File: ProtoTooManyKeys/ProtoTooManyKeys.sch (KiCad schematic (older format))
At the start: 74 parts, among them J1 54104-3031_Oled, J2 AVR-ISP-6, SW1 SW_Push, U1 PRTR5V0U2X, U2 AT90USB1286-AU, U3 PCA9306TDCURQ1, U4 AZ1117CH-3.3TRG1, Y1 16MHz

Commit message: Routing finished
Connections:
- net ROW0: now also U2.34 (PE1); no longer U2.50 (PA1)
- net ROW1: now also U2.33 (PE0); no longer U2.49 (PA2)
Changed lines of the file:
@@
 Text GLabel 4200 4200 2    50   Input ~ 0
 SDA
-Text GLabel 4200 1600 2    50   Input ~ 0
+Text GLabel 2800 3200 0    50   Input ~ 0
 ROW1
-Text GLabel 4200 1500 2    50   Input ~ 0
+Text GLabel 2800 3300 0    50   Input ~ 0
 ROW0
 Text GLabel 4200 3200 2    50   Input ~ 0
@@
 $EndComp
 Wire Wire Line
-	4200 1500 4100 1500
-Wire Wire Line
-	4200 1600 4100 1600
+	2800 3300 2900 3300
+Wire Wire Line
+	2800 3200 2900 3200
 Text GLabel 10350 2400 0    50   Input ~ 0
 RESET
@@
 NoConn ~ 4100 3800
 NoConn ~ 4100 3900
-NoConn ~ 2900 3200
-NoConn ~ 2900 3300
 NoConn ~ 2900 3800
 NoConn ~ 2900 3900
@@
 	1    0    0    -1
 $EndComp
+NoConn ~ 4100 1500
+NoConn ~ 4100 1600
 $EndSCHEMATC

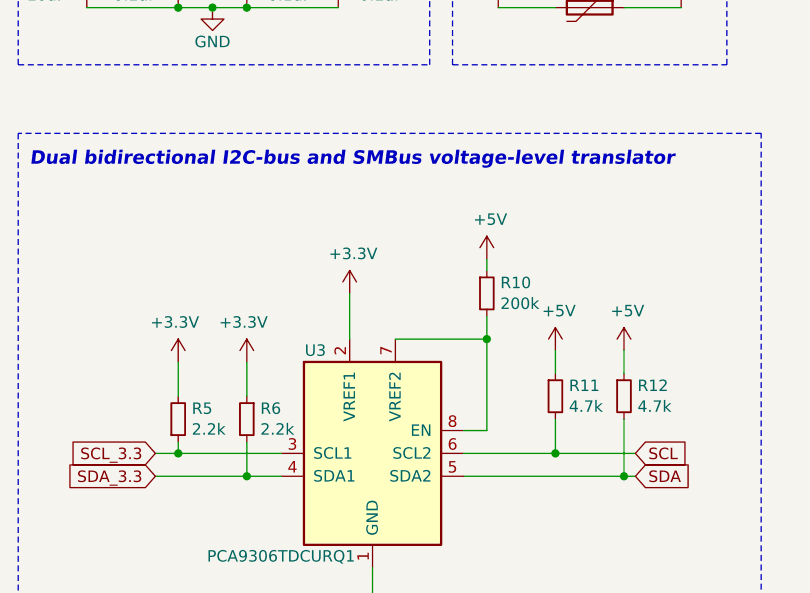
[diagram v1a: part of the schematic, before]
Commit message: Final touches on Proto and added a missing capacitor
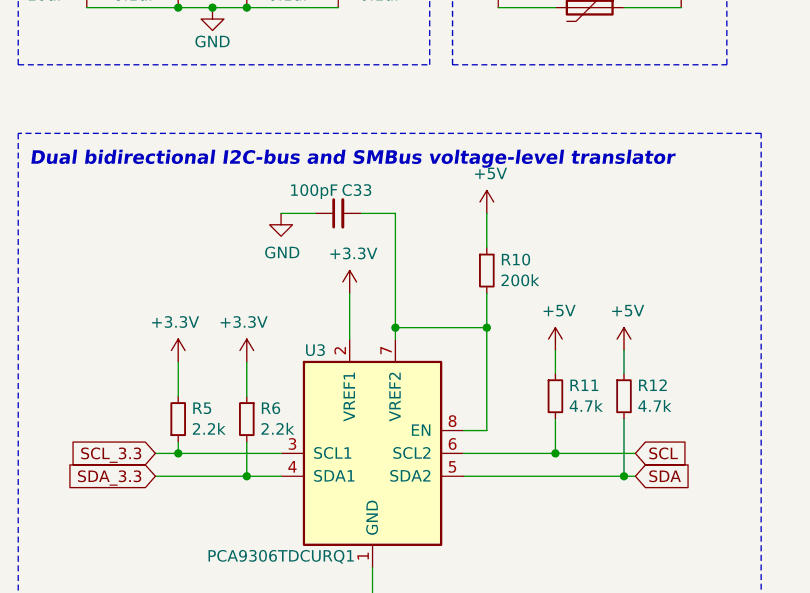
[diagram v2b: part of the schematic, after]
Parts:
- added C33: 100pF, Capacitor_SMD:C_0805_2012Metric, symbol Device:C_Small
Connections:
- net GND: now also C33.1
- net at R10.2, U3.7 (VREF2), U3.8 (EN): now also C33.2
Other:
- moved on the sheet: R10
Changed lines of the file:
@@
 L power:+5V #PWR0128
 U 1 1 606B25C0
-P 2750 7450
-F 0 "#PWR0128" H 2750 7300 50  0001 C CNN
-F 1 "+5V" H 2765 7623 50  0000 C CNN
-F 2 "" H 2750 7450 50  0001 C CNN
-F 3 "" H 2750 7450 50  0001 C CNN
-	1    2750 7450
+P 2750 7250
+F 0 "#PWR0128" H 2750 7100 50  0001 C CNN
+F 1 "+5V" H 2765 7423 50  0000 C CNN
+F 2 "" H 2750 7250 50  0001 C CNN
+F 3 "" H 2750 7250 50  0001 C CNN
+	1    2750 7250
 	1    0    0    -1
 $EndComp
@@
 L Device:R_Small R10
 U 1 1 606BAA09
-P 2750 7600
-F 0 "R10" H 2809 7646 50  0000 L CNN
-F 1 "200k" H 2809 7555 50  0000 L CNN
-F 2 "Resistor_SMD:R_0805_2012Metric" H 2750 7600 50  0001 C CNN
-F 3 "~" H 2750 7600 50  0001 C CNN
-	1    2750 7600
-	1    0    0    -1
-$EndComp
-Wire Wire Line
-	2750 7500 2750 7450
+P 2750 7500
+F 0 "R10" H 2809 7546 50  0000 L CNN
+F 1 "200k" H 2809 7455 50  0000 L CNN
+F 2 "Resistor_SMD:R_0805_2012Metric" H 2750 7500 50  0001 C CNN
+F 3 "~" H 2750 7500 50  0001 C CNN
+	1    2750 7500
+	1    0    0    -1
+$EndComp
 Wire Wire Line
 	2650 8200 2750 8200
-Wire Wire Line
-	2750 8200 2750 7800
 $Comp
 L power:GND #PWR0130
@@
 Wire Wire Line
 	3350 6350 3600 6350
-Wire Wire Line
-	2350 7800 2750 7800
-Connection ~ 2750 7800
-Wire Wire Line
-	2750 7800 2750 7700
 NoConn ~ 10000 7000
 $Comp
@@
 NoConn ~ 4100 1500
 NoConn ~ 4100 1600
+$Comp
+L power:GND #PWR0151
+U 1 1 60FAE119
+P 1850 7250
+F 0 "#PWR0151" H 1850 7000 50  0001 C CNN
+F 1 "GND" H 1855 7077 50  0000 C CNN
+F 2 "" H 1850 7250 50  0001 C CNN
+F 3 "" H 1850 7250 50  0001 C CNN
+	1    1850 7250
+	1    0    0    -1
+$EndComp
+$Comp
+L Device:C_Small C33
+U 1 1 60FB2CC8
+P 2100 7250
+F 0 "C33" V 2200 7100 50  0000 L CNN
+F 1 "100pF" V 2200 7250 50  0000 L CNN
+F 2 "Capacitor_SMD:C_0805_2012Metric" H 2100 7250 50  0001 C CNN
+F 3 "" H 2100 7250 50  0001 C CNN
+	1    2100 7250
+	0    -1   -1   0
+$EndComp
+Wire Wire Line
+	2350 7800 2350 7750
+Wire Wire Line
+	2350 7250 2200 7250
+Wire Wire Line
+	2000 7250 1850 7250
+Wire Wire Line
+	2350 7750 2750 7750
+Connection ~ 2350 7750
+Wire Wire Line
+	2350 7750 2350 7250
+Connection ~ 2750 7750
+Wire Wire Line
+	2750 7750 2750 8200
+Wire Wire Line
+	2750 7400 2750 7250
+Wire Wire Line
+	2750 7600 2750 7750
 $EndSCHEMATC
